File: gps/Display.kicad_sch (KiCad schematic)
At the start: 8 parts, among them U4 HT16k33, U5 7seg_1x1_rgb, U6 7seg_1x1_rgb, U7 7seg_1x1_rgb, U8 KW4-804AGB

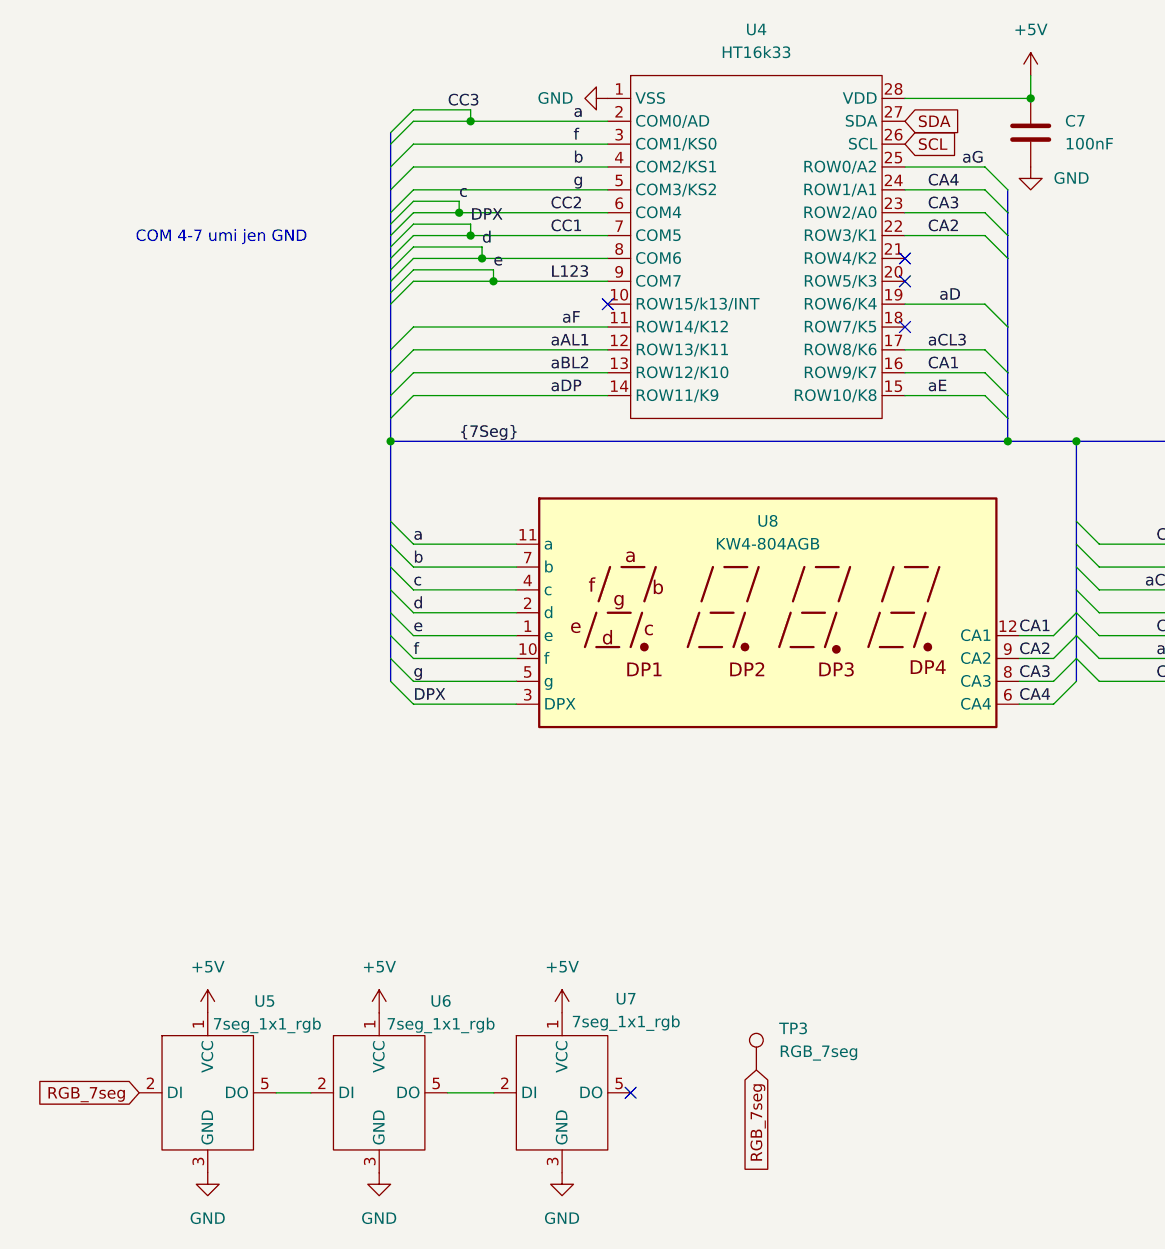
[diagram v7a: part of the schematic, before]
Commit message: added level shifters for i2C and RGB displey,
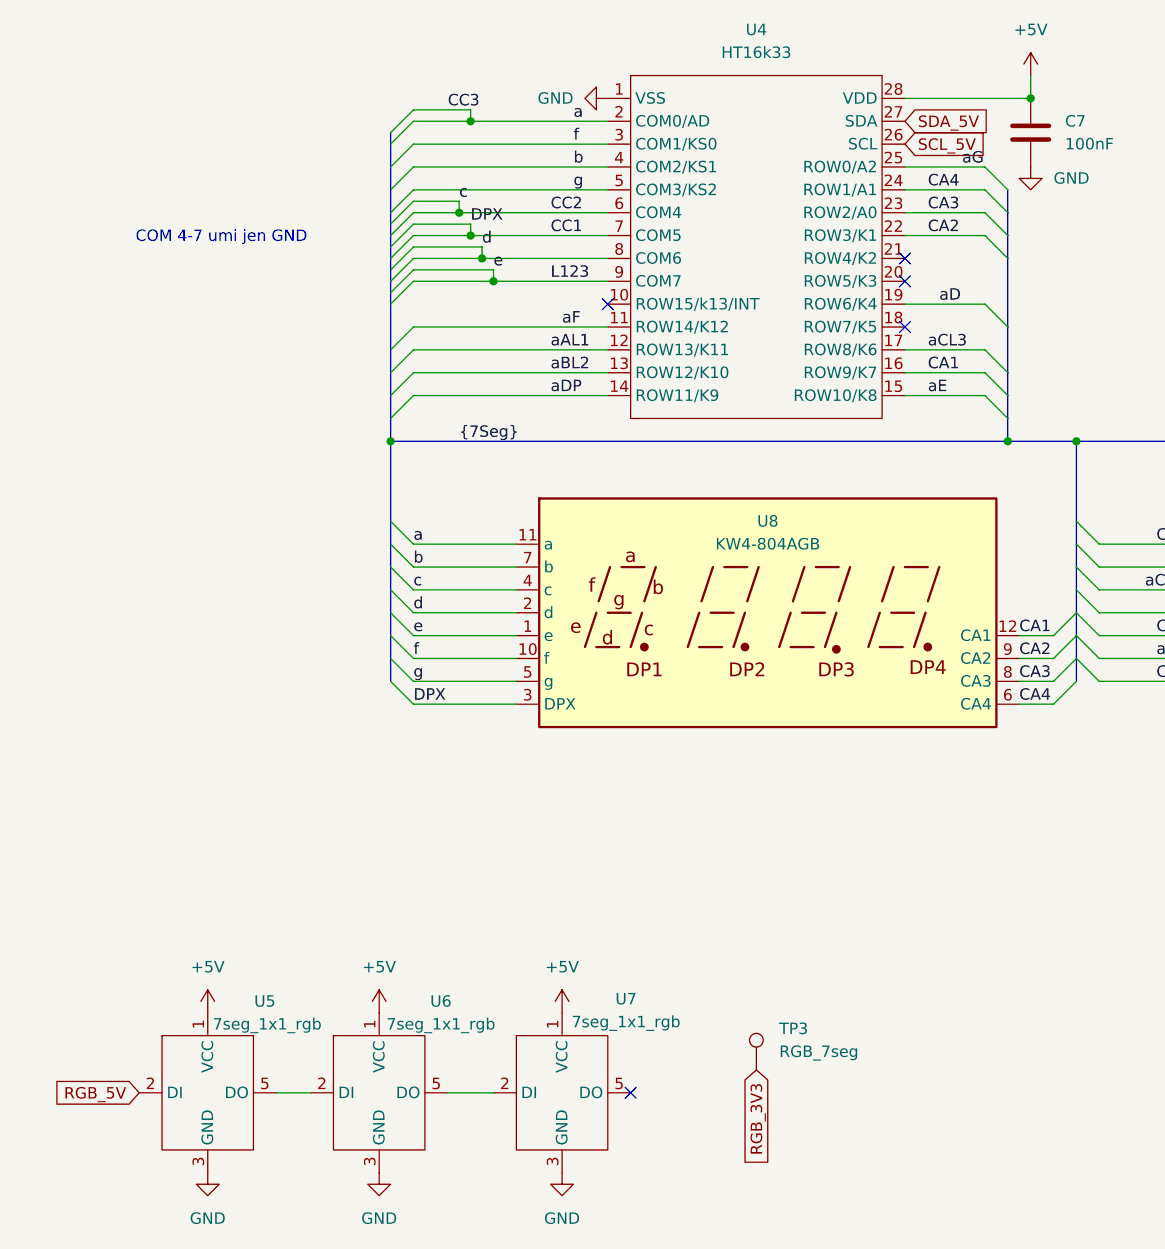
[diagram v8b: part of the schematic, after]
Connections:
- net RGB_7seg renamed RGB_3V3
- net RGB_3V3: no longer U5.2 (DI)
- net SCL renamed SCL_5V
- net SDA renamed SDA_5V
- new net RGB_5V: U5.2 (DI)
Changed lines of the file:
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@@
 		)
 	)
-	(global_label "SCL"
+	(global_label "SCL_5V"
 		(shape input)
 		(at 132.08 52.07 0)
@@
 		)
 		(property "Intersheetrefs" "${INTERSHEET_REFS}"
-			(at 138.0007 51.9906 0)
+			(at 141.8385 52.07 0)
 			(effects
 				(font
@@
 		)
 	)
-	(global_label "RGB_7seg"
+	(global_label "RGB_5V"
+		(shape input)
+		(at 46.99 157.48 180)
+		(fields_autoplaced yes)
+		(effects
+			(font
+				(size 1.27 1.27)
+			)
+			(justify right)
+		)
+		(property "Intersheetrefs" "${INTERSHEET_REFS}"
+			(at 36.9291 157.48 0)
+			(effects
+				(font
+					(size 1.27 1.27)
+				)
+				(justify right)
+				(hide yes)
+			)
+		)
+	)
+	(global_label "SDA_5V"
+		(shape input)
+		(at 132.08 49.53 0)
+		(fields_autoplaced yes)
+		(effects
+			(font
+				(size 1.27 1.27)
+			)
+			(justify left)
+		)
+		(property "Intersheetrefs" "${INTERSHEET_REFS}"
+			(at 141.899 49.53 0)
+			(effects
+				(font
+					(size 1.27 1.27)
+				)
+				(justify left)
+				(hide yes)
+			)
+		)
+	)
+	(global_label "RGB_3V3"
 		(shape input)
 		(at 115.57 154.94 270)
@@
 		)
 		(property "Intersheetrefs" "${INTERSHEET_REFS}"
-			(at 115.57 167.178 90)
+			(at 115.57 166.2104 90)
 			(effects
 				(font
@@
 				(hide yes)
 			)
-		)
-	)
-	(global_label "RGB_7seg"
-		(shape input)
-		(at 46.99 157.48 180)
-		(fields_autoplaced yes)
-		(effects
-			(font
-				(size 1.27 1.27)
-			)
-			(justify right)
-		)
-		(property "Intersheetrefs" "${INTERSHEET_REFS}"
-			(at 34.752 157.48 0)
-			(effects
-				(font
-					(size 1.27 1.27)
-				)
-				(justify right)
-				(hide yes)
-			)
-		)
-	)
-	(global_label "SDA"
-		(shape input)
-		(at 132.08 49.53 0)
-		(fields_autoplaced yes)
-		(effects
-			(font
-				(size 1.27 1.27)
-			)
-			(justify left)
-		)
-		(property "Intersheetrefs" "${INTERSHEET_REFS}"
-			(at 138.0612 49.4506 0)
-			(effects
-				(font
-					(size 1.27 1.27)
-				)
-				(justify left)
-				(hide yes)
-			)
